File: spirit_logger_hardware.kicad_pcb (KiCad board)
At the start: 4 copper layers, 75 x 40 mm, 104 parts, among them J1 PicoBlade, J2 PicoBlade, J3 USB_C_Receptacle, Q1 BSS123, U1 nRF5340-QKAA, U2 MX25R6435F, U3 MCP25625-E/ML, U4 SN74LVC1G00DRY2, U5 74CBTLV3245BQ, U6 LMZ21700SILR, U7 SiP32432DR3, U8 LSM6DSL, X1 Crystal_GND24, X2 Crystal, Y1 16MHz

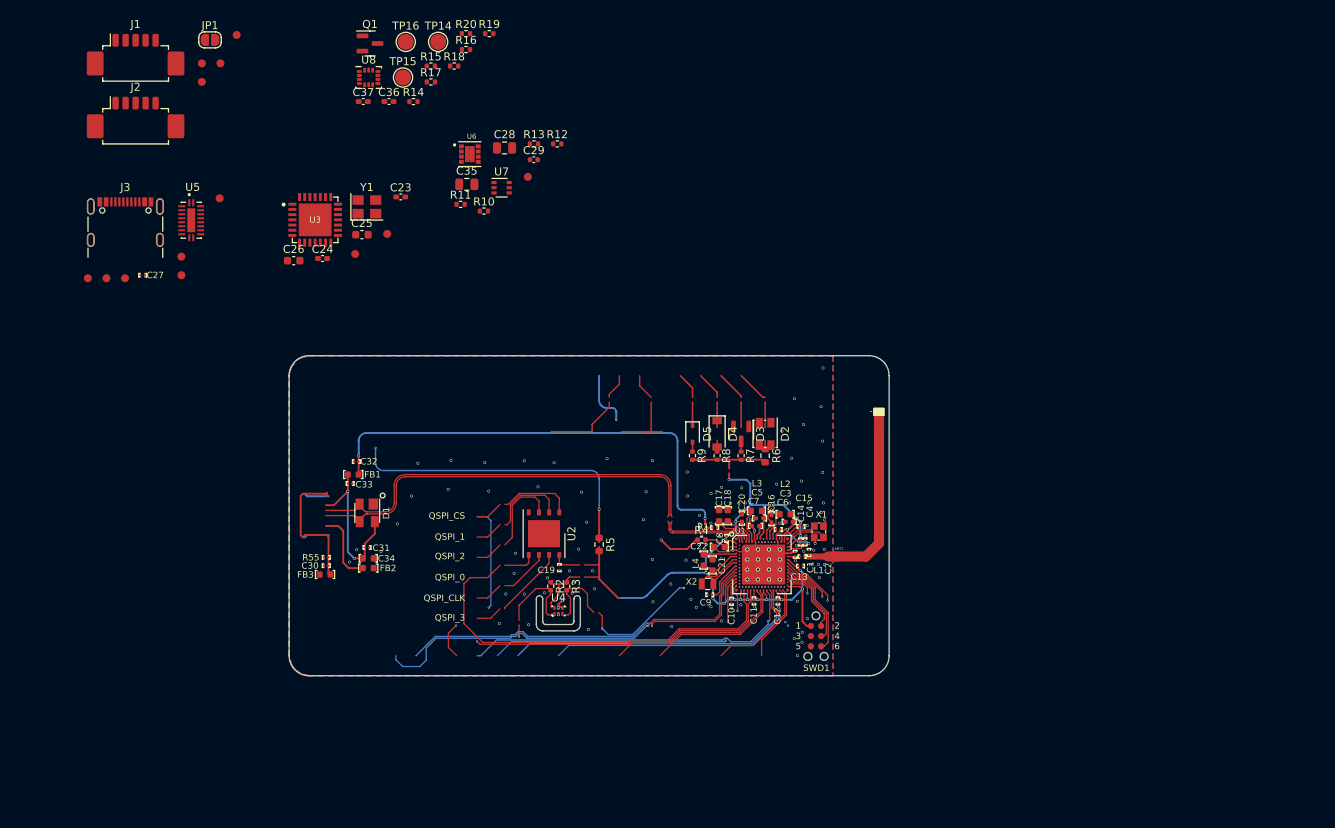
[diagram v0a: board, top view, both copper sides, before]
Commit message: drc updated for pcbway advanced; layout and tidy
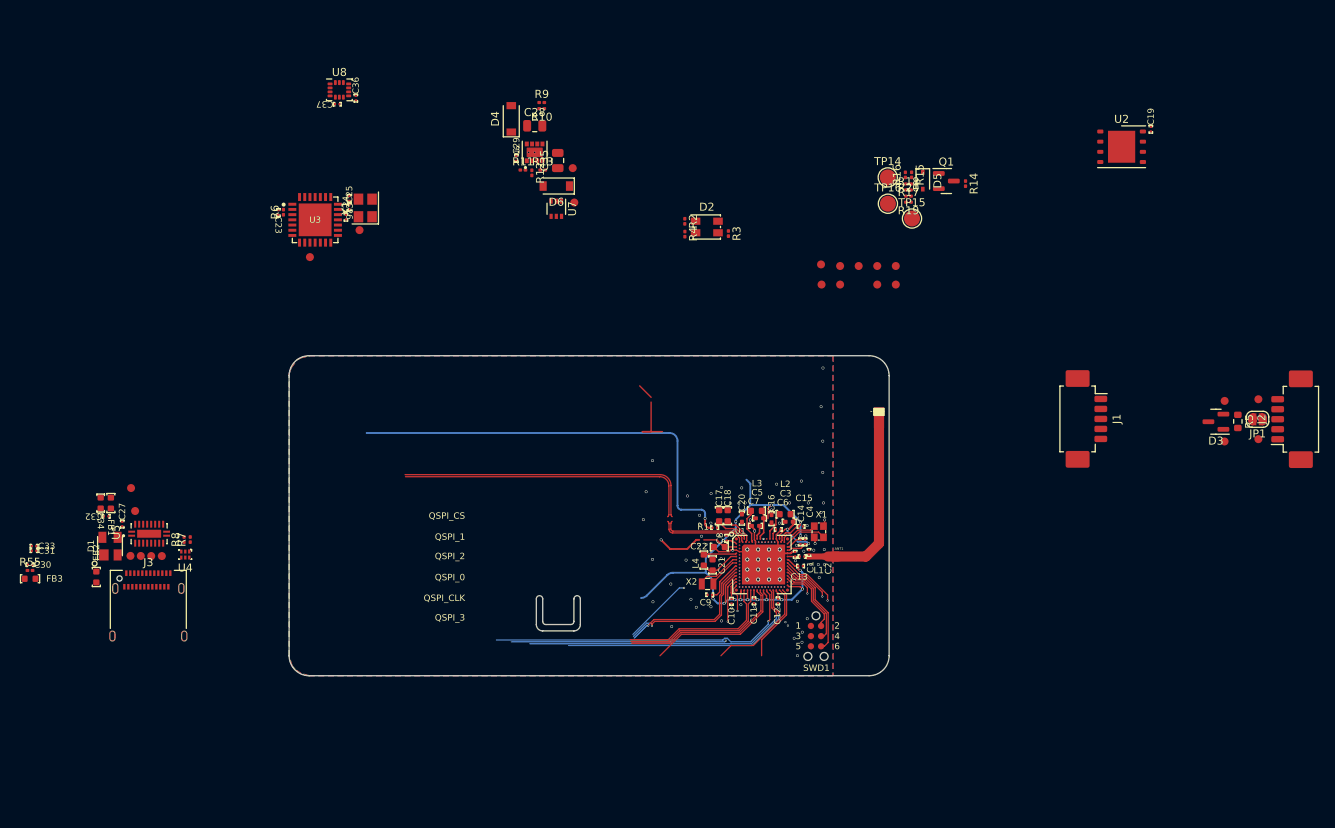
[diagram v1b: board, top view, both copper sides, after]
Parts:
- added D6: MBR0540, Diode_SMD:D_SOD-123, F.Cu at (73.4, 26.3)
- added TP17: TestPoint, tuna-f1sh/jbr-kicad/Misc.pretty:TestPoint_Pad_D1.0mm_Tight, F.Cu at (113.5, 38.6)
- added TP18: TestPoint, tuna-f1sh/jbr-kicad/Misc.pretty:TestPoint_Pad_D1.0mm_Tight, F.Cu at (108.9, 36.3)
- added TP19: TestPoint, tuna-f1sh/jbr-kicad/Misc.pretty:TestPoint_Pad_D1.0mm_Tight, F.Cu at (106.5, 36.1)
- added TP20: TestPoint, tuna-f1sh/jbr-kicad/Misc.pretty:TestPoint_Pad_D1.0mm_Tight, F.Cu at (111.2, 36.3)
- added TP21: TestPoint, tuna-f1sh/jbr-kicad/Misc.pretty:TestPoint_Pad_D1.0mm_Tight, F.Cu at (108.9, 38.6)
- added TP22: TestPoint, tuna-f1sh/jbr-kicad/Misc.pretty:TestPoint_Pad_D1.0mm_Tight, F.Cu at (115.8, 38.6)
- added TP23: TestPoint, tuna-f1sh/jbr-kicad/Misc.pretty:TestPoint_Pad_D1.0mm_Tight, F.Cu at (106.6, 38.6)
- added TP24: TestPoint, tuna-f1sh/jbr-kicad/Misc.pretty:TestPoint_Pad_D1.0mm_Tight, F.Cu at (115.8, 36.3)
- added TP25: TestPoint, tuna-f1sh/jbr-kicad/Misc.pretty:TestPoint_Pad_D1.0mm_Tight, F.Cu at (113.5, 36.3)
- added TP26: TestPoint, tuna-f1sh/jbr-kicad/Misc.pretty:TestPoint_Pad_D1.0mm_Tight, F.Cu at (75.7, 28.4)
- C23, C24, C36, C37: footprint Capacitor_SMD.pretty:C_0402_1005Metric_Pad0.74x0.62mm_HandSolder -> MCU_Nordic_Accessory:C_0201
- C25, C26: footprint Capacitor_SMD.pretty:C_0603_1608Metric -> MCU_Nordic_Accessory:C_0201
- C28, C35: footprint Capacitor_SMD.pretty:C_0805_2012Metric -> Capacitor_SMD:C_0805_2012Metric
- C29: footprint Capacitor_SMD.pretty:C_0402_1005Metric -> MCU_Nordic_Accessory:C_0201
- D2: footprint LED_SMD.pretty:LED_Kingbright_AAA3528ESGCT -> LED_SMD:LED_Kingbright_AAA3528ESGCT
- D3, Q1: footprint Package_TO_SOT_SMD.pretty:SOT-23 -> Package_TO_SOT_SMD:SOT-23
- D4: footprint Diode_SMD.pretty:D_SOD-123 -> Diode_SMD:D_SOD-123
- D5: footprint Diode_SMD.pretty:D_SOD-323 -> Diode_SMD:D_SOD-323
- J1, J2: footprint Connector_Molex.pretty:Molex_PicoBlade_53261-0571_1x05-1MP_P1.25mm_Horizontal -> Connector_Molex:Molex_PicoBlade_53261-0571_1x05-1MP_P1.25mm_Horizontal
- J3: footprint Connector_USB.pretty:USB_C_Receptacle_GCT_USB4105-xx-A_16P_TopMnt_Horizontal -> Connector_USB:USB_C_Receptacle_Amphenol_12401610E4-2A
- JP1: footprint Jumper.pretty:SolderJumper-2_P1.3mm_Open_RoundedPad1.0x1.5mm -> Jumper:SolderJumper-2_P1.3mm_Open_RoundedPad1.0x1.5mm
- R10, R13, R14, R15, R16, R17, R18, R19, R2, R20, R3, R4, R7, R8, R9: footprint Resistor_SMD.pretty:R_0402_1005Metric -> Resistor_SMD:R_0201_0603Metric
- R11: value 44.2k -> 40k; footprint Resistor_SMD.pretty:R_0402_1005Metric -> Resistor_SMD:R_0201_0603Metric
- R12: value 232k -> 240k; footprint Resistor_SMD.pretty:R_0402_1005Metric -> Resistor_SMD:R_0201_0603Metric
- R5: footprint Resistor_SMD.pretty:R_0603_1608Metric -> Resistor_SMD:R_0603_1608Metric
- R55: footprint MCU_Nordic_Accessory:R_0201 -> Resistor_SMD:R_0201_0603Metric
- R6: footprint Resistor_SMD.pretty:R_0603_1608Metric -> Resistor_SMD:R_0201_0603Metric
- TP1, TP10, TP11, TP12, TP13, TP2, TP3, TP4, TP5, TP6, TP7, TP8, TP9: footprint tunaf1sh/misc.pretty:TestPoint_Pad_D1.0mm_Tight -> tuna-f1sh/jbr-kicad/Misc.pretty:TestPoint_Pad_D1.0mm_Tight
- TP14, TP15, TP16: footprint TestPoint.pretty:TestPoint_Pad_D2.0mm -> TestPoint:TestPoint_Pad_D2.0mm
- U2: footprint Package_SON.pretty:WSON-8-1EP_6x5mm_P1.27mm_EP3.4x4mm -> Package_SON:WSON-8-1EP_6x5mm_P1.27mm_EP3.4x4mm
- U3: footprint tunaf1sh/QFN.pretty:QFN-28L -> tuna-f1sh/jbr-kicad/QFN.pretty:QFN-28L
- U5: footprint tunaf1sh/snapeda.pretty:QFN50P450X250X100-21N -> tuna-f1sh/jbr-kicad/SnapEDA.pretty:QFN50P450X250X100-21N
- U6: footprint tunaf1sh/snapeda.pretty:CONV_TPS82140SILR -> tuna-f1sh/jbr-kicad/SnapEDA.pretty:CONV_TPS82140SILR
- U7: footprint Package_TO_SOT_SMD.pretty:SOT-363_SC-70-6 -> Package_TO_SOT_SMD:SOT-363_SC-70-6
- U8: footprint Package_LGA.pretty:LGA-14_3x2.5mm_P0.5mm_LayoutBorder3x4y -> Package_LGA:LGA-14_3x2.5mm_P0.5mm_LayoutBorder3x4y
- Y1: footprint Crystal.pretty:Crystal_SMD_3225-4Pin_3.2x2.5mm -> Crystal:Crystal_SMD_3225-4Pin_3.2x2.5mm
- moved J2 149.8 mm to (166.0, 55.4), turned to 90 degrees
- moved JP1 139.3 mm to (161.1, 55.5), turned to 180 degrees
- moved TP4 138.6 mm to (161.2, 52.9)
- moved TP3 138.0 mm to (161.2, 57.9)
- moved TP2 135.5 mm to (156.9, 58.2)
- moved TP1 131.7 mm to (156.9, 53.1)
- moved J1 126.5 mm to (139.1, 55.4), turned to -90 degrees
- moved C19 92.0 mm to (147.7, 19.2), turned to 90 degrees
- moved U2 86.9 mm to (144.1, 21.4), turned to 0 degrees
- moved R5 81.3 mm to (158.6, 55.7)
- moved Q1 74.1 mm to (122.2, 25.7)
- moved R14 69.8 mm to (124.5, 26.0), turned to -90 degrees
- moved R7 69.7 mm to (27.6, 70.5), turned to 90 degrees
- moved R6 67.5 mm to (39.3, 29.6), turned to 90 degrees
- moved R8 67.4 mm to (26.9, 70.5), turned to 90 degrees
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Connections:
- net /P0.02/NFC1 renamed /Radio Sheet/P0.02/NFC1
- net /P0.03/NFC2 renamed /Radio Sheet/P0.03/NFC2
- net /P0.04/AIN0 renamed /Radio Sheet/P0.04/AIN0
- net /P0.05/AIN1 renamed /Radio Sheet/P0.05/AIN1
- net /P0.08/TRACEDATA_3 renamed /Radio Sheet/P0.08/TRACEDATA_3
- net /P0.09/TRACEDATA_2 renamed /Radio Sheet/P0.09/TRACEDATA_2
- net /P0.10/TRACEDATA_1 renamed /Radio Sheet/P0.10/TRACEDATA_1
- net /P0.11/TRACEDATA_0 renamed /Radio Sheet/P0.11/TRACEDATA_0
- net /P0.12/TRACECLK renamed /Radio Sheet/P0.12/TRACECLK
- net /P0.20 renamed /Radio Sheet/P0.20
- net /P0.25/AIN4 renamed /Radio Sheet/P0.25/AIN4
- net /P0.27/AIN6 renamed /Radio Sheet/P0.27/AIN6
- net /P0.28/AIN7 renamed /Radio Sheet/P0.28/AIN7
- net /P0.29 renamed /Radio Sheet/P0.29
- net /P1.02/I2C renamed /Radio Sheet/P1.02/I2C
- net /P1.03/I2C renamed /Radio Sheet/P1.03/I2C
- net /P1.05 renamed /Radio Sheet/P1.05
- net /P1.06 renamed /Radio Sheet/P1.06
- net /P1.07 renamed /Radio Sheet/P1.07
- net /P1.08 renamed /Radio Sheet/P1.08
- C10 pad 1: VCC -> Net-(C10-Pad1)
- C11 pad 1: VCC -> Net-(C10-Pad1)
- C12 pad 1: VCC -> Net-(C10-Pad1)
- C13 pad 1: VCC -> Net-(C10-Pad1)
- C14 pad 1: VCC -> Net-(C10-Pad1)
- C15 pad 1: VCC -> Net-(C10-Pad1)
- C22 pad 1: /Radio Sheet/VDDH -> +5V
- C23 pad 2: VDD -> VCC
- C35 pad 1: /Power/VOUT -> /Power/DCDC_VOUT
- C8 pad 1: VCC -> Net-(C10-Pad1)
- C9 pad 1: VCC -> Net-(C10-Pad1)
- R13 pad 2: /Power/VOUT -> /Power/DCDC_VOUT
- R6 pad 1: VDD -> VCC
- TP13 pad 1: /Power/VOUT -> /Power/DCDC_VOUT
- U1 pad AC1: VCC -> Net-(C10-Pad1)
- U1 pad AG1: VCC -> Net-(C10-Pad1)
- U1 pad AJ31: VCC -> Net-(C10-Pad1)
- U1 pad AL11: VCC -> Net-(C10-Pad1)
- U1 pad AL13: /P0.19 -> /P0.19/SDA
- U1 pad AL15: /P0.21 -> /P0.21/SCL
- U1 pad AL17: VCC -> Net-(C10-Pad1)
- U1 pad AL25: VCC -> Net-(C10-Pad1)
- U1 pad AL3: VCC -> Net-(C10-Pad1)
- U1 pad AL7: VCC -> Net-(C10-Pad1)
- U1 pad B28: VCC -> Net-(C10-Pad1)
- U1 pad C1: VCC -> Net-(C10-Pad1)
- U1 pad E1: /Radio Sheet/VDDH -> +5V
- U1 pad E31: VCC -> Net-(C10-Pad1)
- U1 pad N31: VCC -> Net-(C10-Pad1)
- U1 pad U1: VCC -> Net-(C10-Pad1)
- U3 pad 11: VDD -> VCC
- U3 pad 3: VDD -> VCC
- U6 pad 4: /Power/VOUT -> /Power/DCDC_VOUT
- U7 pad 1: /Radio Sheet/VDDH -> +5V
- U7 pad 2: Net-(U7-Pad2) -> GND
- U7 pad 3: /Power/VOUT -> /Power/DCDC_VOUT
- U7 pad 5: Net-(U7-Pad2) -> GND
- U8 pad 13: /P0.21/I2C -> /P0.21/SCL
- U8 pad 14: /P0.19/I2C -> /P0.19/SDA
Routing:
- net VCC: track 112.8 -> 5.03 mm, vias 17 -> 0
- net Net-(C10-Pad1): track 0.00 -> 85.1 mm, vias 0 -> 15
- net Net-(JP1-Pad2): track 47.8 -> 0.00 mm, vias 2 -> 0
- net /P0.13/QSPI_0: track 55.9 -> 19.5 mm
- net /P0.16/QSPI_3: track 54.5 -> 19.7 mm, vias 1 -> 0
- net /Radio Sheet/P0.02/NFC1: track 52.0 -> 18.5 mm
- net /P0.18/QSPI_CS: track 68.0 -> 35.6 mm, vias 2 -> 1
- net /Radio Sheet/P0.28/AIN7: track 66.6 -> 34.2 mm
- net /Radio Sheet/P0.29: track 68.9 -> 37.8 mm
- net /Radio Sheet/P1.03/I2C: track 46.7 -> 16.3 mm, vias 4 -> 2
- net /P0.14/QSPI_1: track 62.6 -> 33.0 mm
- net /Radio Sheet/P0.03/NFC2: track 47.4 -> 18.7 mm
- net /P0.15/QSPI_2: track 61.4 -> 34.0 mm
- net /P1.01: track 56.7 -> 31.5 mm
- net /Radio Sheet/P1.02/I2C: track 46.8 -> 22.7 mm, vias 2 -> 1
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
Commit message: steps added, before shorten
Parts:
- removed TP22, TP23: TestPoint, tuna-f1sh/jbr-kicad/Misc.pretty:TestPoint_Pad_D1.0mm_Tight
- C23, C24, C25, C26, D3, J1, JP1, R5, R6, TP14, TP15, TP16, U3, Y1: moved to B.Cu
- U6: footprint tuna-f1sh/jbr-kicad/SnapEDA.pretty:CONV_TPS82140SILR -> tuna-f1sh/jbr-kicad/SnapEDA.pretty:Texas_Instruments-SIL0008E-0-0-MFG
- moved FB2 89.4 mm to (103.5, 92.8), turned to 0 degrees
- moved R55 88.7 mm to (93.8, 95.2), turned to 90 degrees
- moved FB3 88.6 mm to (93.5, 97.2), turned to -90 degrees
- moved C30 88.1 mm to (93.0, 95.3), turned to 90 degrees
- moved TP12 87.5 mm to (105.5, 88.9)
- moved C33 87.4 mm to (94.3, 86.1), turned to -90 degrees
- moved C31 86.8 mm to (93.7, 86.1), turned to -90 degrees
- moved C34 81.2 mm to (95.2, 85.5)
- moved TP9 81.0 mm to (98.6, 92.8)
- moved C27 79.9 mm to (96.4, 88.9)
- moved R8 79.8 mm to (104.0, 91.2), turned to -90 degrees
- moved TP8 79.8 mm to (101.3, 92.8)
- moved U5 79.8 mm to (99.7, 90.0)
- moved J3 79.8 mm to (99.6, 100.0)
- moved TP7 79.8 mm to (100.0, 92.8)
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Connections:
- net /CAN_H renamed /CAN_P
- net /CAN_L renamed /CAN_N
- C10 pad 1: Net-(C10-Pad1) -> VCC
- C11 pad 1: Net-(C10-Pad1) -> VCC
- C12 pad 1: Net-(C10-Pad1) -> VCC
- C13 pad 1: Net-(C10-Pad1) -> VCC
- C14 pad 1: Net-(C10-Pad1) -> VCC
- C15 pad 1: Net-(C10-Pad1) -> VCC
- C25 pad 1: Net-(C25-Pad1) -> GND
- C25 pad 2: Net-(C25-Pad2) -> Net-(U3-OSC2)
- C26 pad 1: Net-(C25-Pad1) -> GND
- C8 pad 1: Net-(C10-Pad1) -> VCC
- C9 pad 1: Net-(C10-Pad1) -> VCC
- J3 pad A2: Net-(J3-PadA2) -> /USB/TX_P
- J3 pad A3: Net-(J3-PadA3) -> /USB/TX_N
- R12 pad 2: /Power/VOUT -> /Power/DCDC_VOUT
- TP10 pad 1: Net-(J3-PadA2) -> /USB/TX_P
- TP9 pad 1: Net-(J3-PadA3) -> /USB/TX_N
- U1 pad AC1: Net-(C10-Pad1) -> VCC
- U1 pad AG1: Net-(C10-Pad1) -> VCC
- U1 pad AJ31: Net-(C10-Pad1) -> VCC
- U1 pad AL11: Net-(C10-Pad1) -> VCC
- U1 pad AL17: Net-(C10-Pad1) -> VCC
- U1 pad AL25: Net-(C10-Pad1) -> VCC
- U1 pad AL3: Net-(C10-Pad1) -> VCC
- U1 pad AL7: Net-(C10-Pad1) -> VCC
- U1 pad B28: Net-(C10-Pad1) -> VCC
- U1 pad C1: Net-(C10-Pad1) -> VCC
- U1 pad E31: Net-(C10-Pad1) -> VCC
- U1 pad N31: Net-(C10-Pad1) -> VCC
- U1 pad U1: Net-(C10-Pad1) -> VCC
- U3 pad 20: Net-(C25-Pad1) -> Net-(U3-OSC2)
- U5 pad 2: Net-(J3-PadA3) -> /USB/TX_P
- U5 pad 3: Net-(J3-PadA2) -> /USB/TX_N
- U6 pad 6: /Power/VOUT -> /Power/DCDC_VOUT
- Y1 pad 1: Net-(C25-Pad2) -> Net-(U3-OSC2)
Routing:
- net VCC: track 5.03 -> 137.1 mm, vias 0 -> 21
- net Net-(C10-Pad1): track 85.1 -> 0.00 mm, vias 15 -> 0
- net /USB/VBUS_CONN: track 0.00 -> 51.3 mm, vias 0 -> 2
- net /Radio Sheet/P0.05/AIN1: track 47.3 -> 0.00 mm, vias 1 -> 0
- net /Radio Sheet/P0.04/AIN0: track 42.4 -> 0.00 mm, vias 1 -> 0
- net /Radio Sheet/P0.29: track 37.8 -> 0.00 mm, vias 1 -> 0
- net /Radio Sheet/P1.05: track 37.5 -> 0.00 mm, vias 2 -> 0
- net /P1.10: track 37.9 -> 0.92 mm, vias 1 -> 2
- net /Radio Sheet/P1.06: track 36.0 -> 0.00 mm, vias 1 -> 0
- net /Radio Sheet/P0.28/AIN7: track 34.2 -> 0.00 mm, vias 1 -> 0
- net /P0.07/AIN3: track 56.9 -> 24.7 mm, vias 1 -> 2
- net /Radio Sheet/P1.08: track 31.5 -> 0.00 mm, vias 1 -> 0
- net /P1.00: track 39.8 -> 8.45 mm, vias 1 -> 2
- net /CAN_N: track 0.00 -> 31.3 mm, vias 0 -> 2
- net /CAN_P: track 0.00 -> 30.6 mm, vias 0 -> 2
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- added copper zone on F.Cu, net /Power/DCDC_VOUT
- added copper zone on F.Cu, net Net-(D4-K)
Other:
- board size 75 x 40 mm -> 25 x 67 mm

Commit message: layout before hide
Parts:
- moved TP3 12.6 mm to (93.7, 46.6)
- moved R10 9.84 mm to (95.1, 49.2)
- moved R9 9.84 mm to (95.9, 49.2)
- moved TP4 5.93 mm to (92.1, 46.6)
- moved C28 4.74 mm to (106.4, 52.4)
- moved D6 4.74 mm to (98.9, 55.1)
- moved TP26 4.74 mm to (96.8, 57.4)
- moved U6 4.74 mm to (103.1, 52.4)
- moved U7 4.74 mm to (96.0, 55.1)
- moved C35 4.72 mm to (101.9, 55.4)
- moved R13 4.71 mm to (100.7, 53.5)
- moved R12 4.61 mm to (100.4, 52.0)
- moved R11 4.58 mm to (100.7, 50.8)
- moved TP13 4.57 mm to (100.7, 57.2)
- moved C29 4.42 mm to (101.9, 50.0)
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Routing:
- net /P1.10: track 0.92 -> 21.6 mm
- net /P1.09: track 0.94 -> 16.7 mm, vias 1 -> 2
- net /Power/DCDC_VOUT: track 17.4 -> 12.9 mm
- net GND: track 39.4 -> 43.2 mm, vias 66 -> 59
- net +5V: track 29.9 -> 26.4 mm
- net +12V: track 17.9 -> 20.8 mm
- net /CAN/TXD: track 11.5 -> 14.0 mm
- net /P0.26/AIN5: track 29.9 -> 32.0 mm
- net /P1.15: track 17.7 -> 19.6 mm
- net /USB/VBUS_CONN: track 51.3 -> 49.4 mm
- net VBUS: track 40.8 -> 39.2 mm
- net /Radio Sheet/D_P: track 52.5 -> 50.9 mm
- net /CAN_P: track 30.6 -> 29.0 mm
- net /Radio Sheet/D_N: track 51.9 -> 50.4 mm
- net /SWDCLK: track 23.9 -> 22.5 mm
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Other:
- board size 25 x 67 mm -> 25 x 61.5 mm
- board text removed: "GND"
- board text removed: "P0.02/NFC1"
- board text removed: "P0.03/NFC2"
- board text removed: "P0.04/AIN0"
- board text removed: "P0.05/AIN1"
- board text removed: "P0.06/AIN2"
- board text removed: "P0.07/AIN3"
- board text removed: "P0.20"
- board text removed: "P0.21"
- board text removed: "P0.22"
- board text removed: "P0.23"
- board text removed: "P0.24"
- board text removed: "P0.25/AIN4"
- board text removed: "P0.26/AIN5"
- board text removed: "P0.27/AIN6"
- board text removed: "P0.28/AIN7"
- board text removed: "P0.29"
- board text removed: "P0.30"
- board text removed: "P0.31"
- board text removed: "P1.00"
- board text removed: "P1.01"
- board text removed: "P1.02/I2C"
- board text removed: "P1.03/I2C"
- board text removed: "P1.05"
- board text removed: "P1.06"
- board text removed: "P1.10"
- board text removed: "P1.11"
- board text removed: "P1.12"
- board text removed: "P1.13"
- board text removed: "P1.14"
- board text removed: "P1.15"
- board text removed: "QSPI_0"
- board text removed: "QSPI_1"
- board text removed: "QSPI_2"
- board text removed: "QSPI_3"
- board text removed: "QSPI_CLK"
- board text removed: "QSPI_CS"
- board text removed: "VDDH_EXT"
- board text removed: "VDD_EXT"

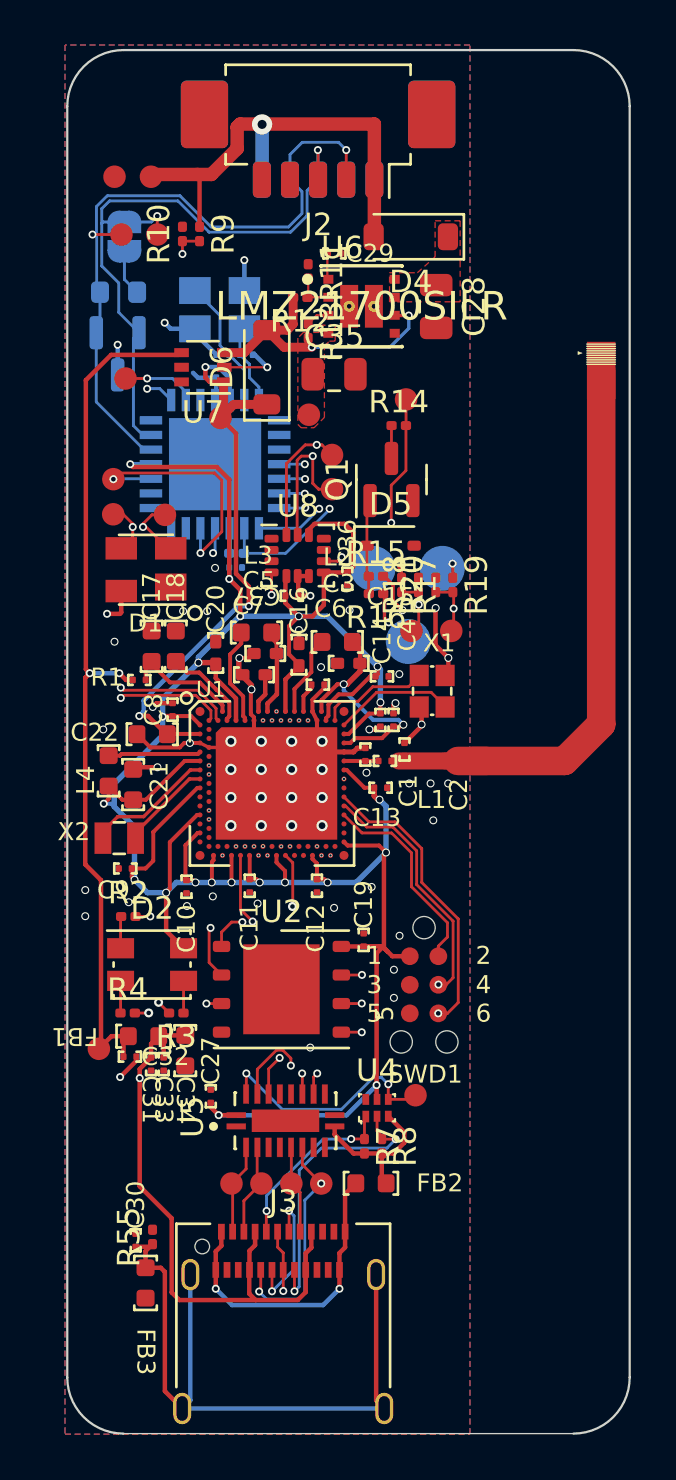
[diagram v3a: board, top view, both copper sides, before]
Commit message: shortened board with usb-c
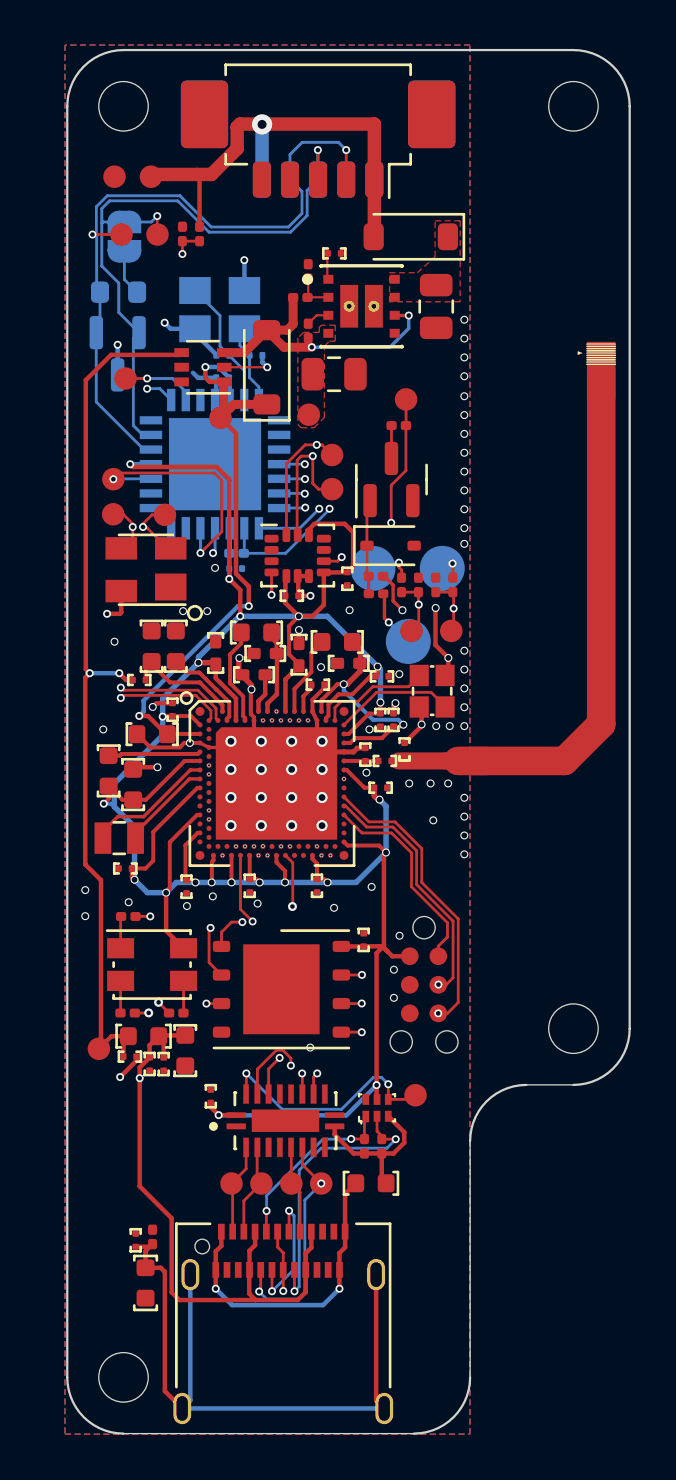
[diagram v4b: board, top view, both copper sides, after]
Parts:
- added H1: MountingHole, MountingHole:MountingHole_2.2mm_M2_DIN965, F.Cu at (112.5, 84.5)
- added H2: MountingHole, MountingHole:MountingHole_2.2mm_M2_DIN965, F.Cu at (92.5, 100.0)
- added H3: MountingHole, MountingHole:MountingHole_2.2mm_M2_DIN965, F.Cu at (112.5, 43.5)
- added H4: MountingHole, MountingHole:MountingHole_2.2mm_M2_DIN965, F.Cu at (92.5, 43.5)
- moved C26 0.43 mm to (98.4, 54.6)
- moved C31 0.07 mm to (93.7, 86.1)
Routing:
- net GND: track 43.2 -> 43.0 mm, vias 59 -> 83
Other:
- outline, holes or cut-outs redrawn
- board text removed: "4"
- board text removed: "5"
